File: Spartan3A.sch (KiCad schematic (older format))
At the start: 29 parts, among them P1 JTAG_FPGA, Q1 Q_NMOS_DSG, U1 XC3S50A/VQ100, U6 M25P20, X1 XO-14S

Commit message: Layouting
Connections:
- net BTN2: now reaches U1.82 (IP_0/VREF_0)
- net BTN1: now reaches U1.97 (IP_0)
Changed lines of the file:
@@
 Text Label 5750 4500 0    60   ~ 0
 GPIO010
+Text Label 5750 4800 0    60   ~ 0
+BTN1
+Text Label 5750 4900 0    60   ~ 0
+BTN2
 $EndSCHEMATC

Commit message: Layout
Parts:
- removed X1: XO-14S, symbol XO-14S
- added C17, C19, C21: 1µF, Capacitors_SMD:C_0805_HandSoldering, symbol C
- added U7: XO53, Oscillator__Crystal_SMD:Oscillator_XO53, symbol XO53
- C29: footprint Capacitors_SMD:C_0603_HandSoldering -> Capacitors_SMD:C_0805_HandSoldering
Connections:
- net GND: now also C17.2, C19.2, C21.2, U7.2 (GND)
- net PROG_B: no longer R1.1, U1.100 (PROG_B)
- net VCC: now also C17.1, U7.1 (VCC)
- net VCC_AUX: now also C19.1
- net VCC_INT: now also C21.1
- net Clock_In: no longer names the net of U1.90 (IO_0/GCLK11)
- net Clock_In: now also U7.3 (Clock)
- new net: R1.1, U1.100 (PROG_B)
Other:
- moved on the sheet: C1, C10, C11, C12, C13, C14, C8, C9

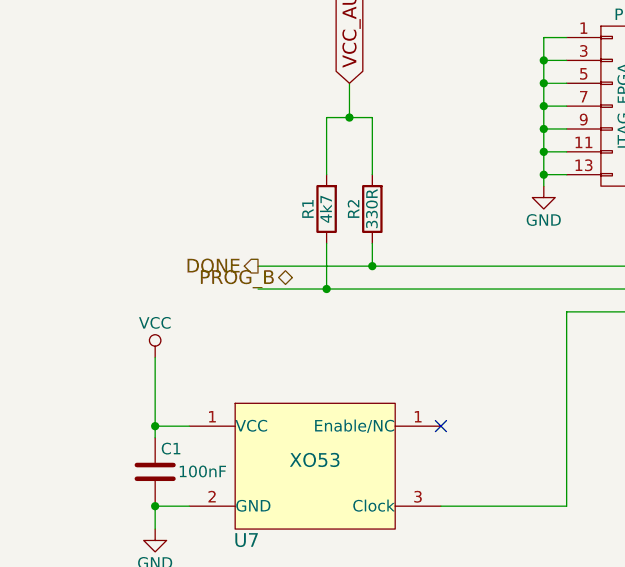
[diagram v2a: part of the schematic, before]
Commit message: Additional Caps at VCC, Layout
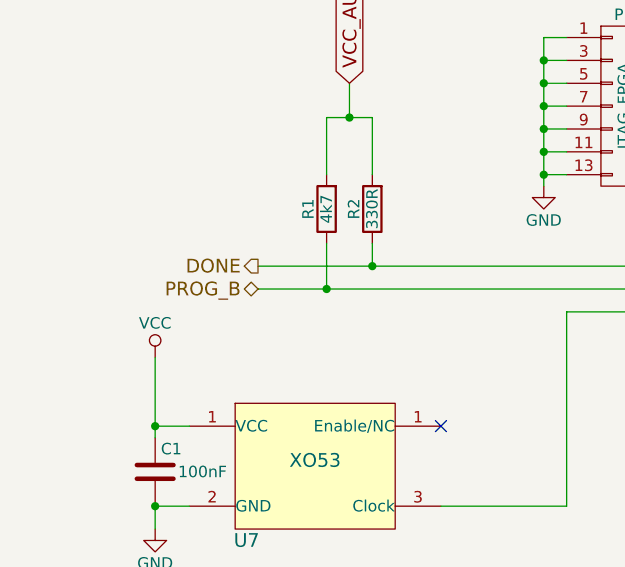
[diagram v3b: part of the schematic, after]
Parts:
- C29: footprint Capacitors_SMD:C_0805_HandSoldering -> Capacitors_SMD:C_0603_HandSoldering
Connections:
- net PROG_B: now also R1.1, U1.100 (PROG_B)
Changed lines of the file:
@@
 F 0 "C29" H 3875 7300 50  0000 L CNN
 F 1 "100nF" H 3875 7100 50  0000 L CNN
-F 2 "Capacitors_SMD:C_0805_HandSoldering" H 3888 7050 50  0001 C CNN
+F 2 "Capacitors_SMD:C_0603_HandSoldering" H 3888 7050 50  0001 C CNN
 F 3 "" H 3850 7200 50  0000 C CNN
 	1    3850 7200
@@
 Text HLabel 2850 3150 0    60   Output ~ 0
 DONE
-Text HLabel 3000 3200 0    60   BiDi ~ 0
+Text HLabel 2850 3250 0    60   BiDi ~ 0
 PROG_B
 $Comp
